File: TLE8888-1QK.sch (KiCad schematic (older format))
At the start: 40 parts, among them Q1 IPD30N06S2L-23, U2 TLE8888QK

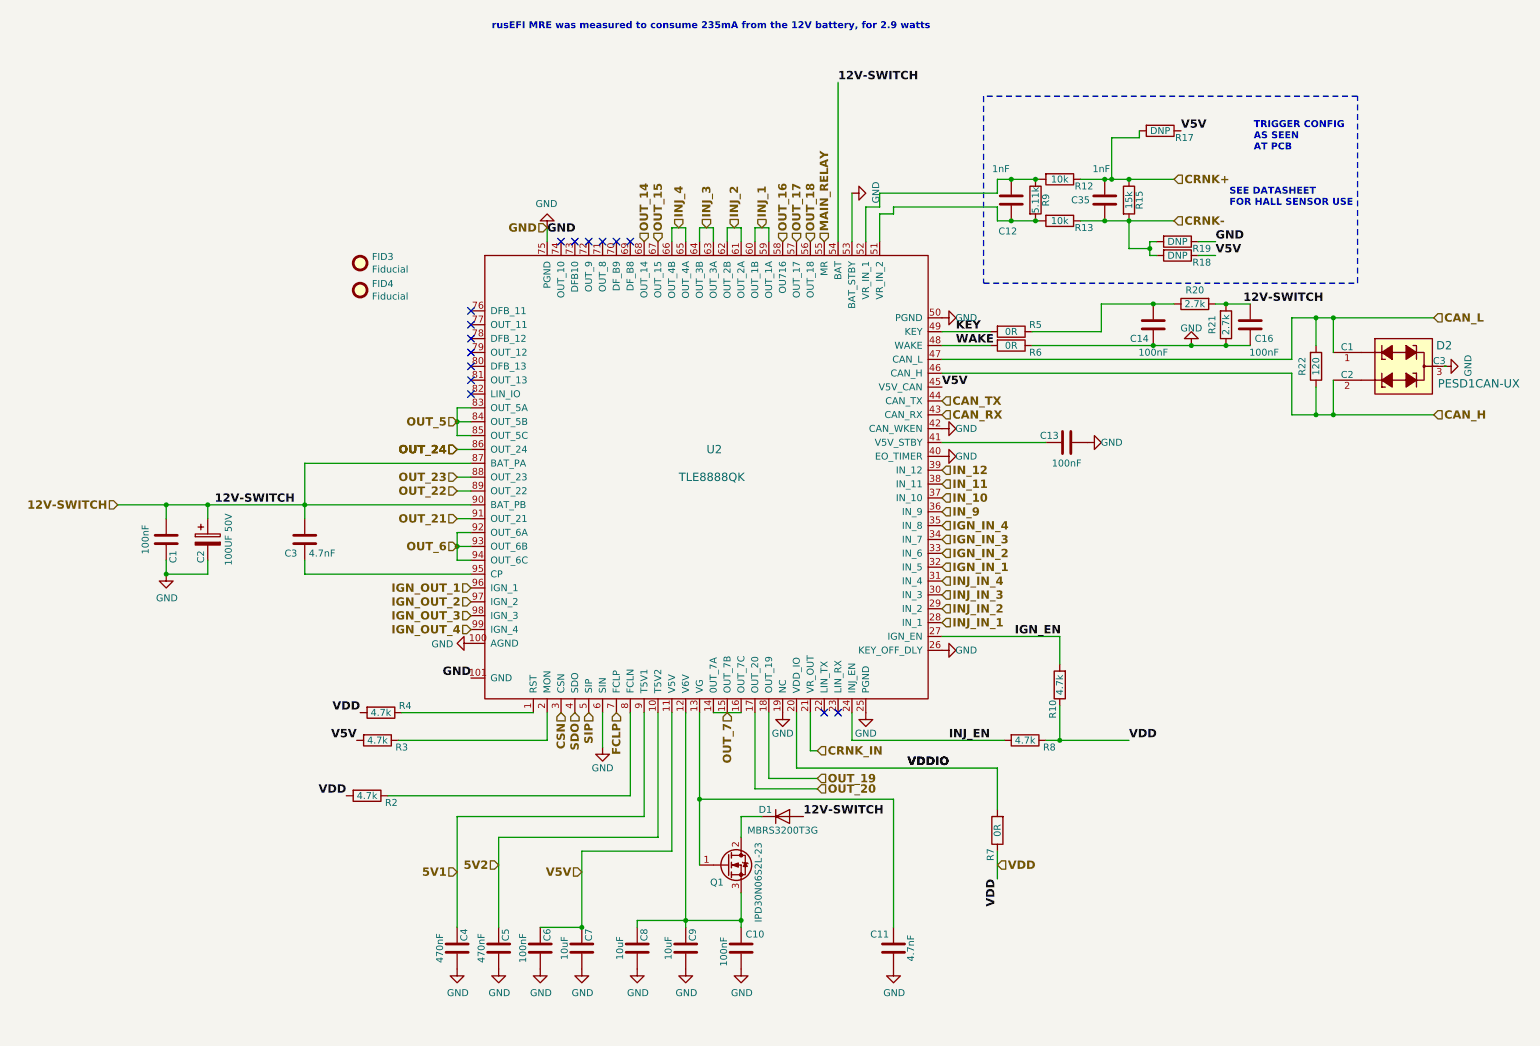
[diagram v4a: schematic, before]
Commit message: Significant revision of schematic and layout:
Added reverse voltage protection.
Split 12V supply into a 12V-Key (ignition) pin and a 12V-MRel (supply from
main relay) pin.  The 12V main relay is controlled by the MRel pin to protect against reverse voltage and over-voltage.

The board can optionally draw under 1mA from the main relay coil to power
standby features, including CAN monitoring.

Increased the size of several resistors, notably ignition output resistors
and CAN termination, to handle typical power draw.

Changed resistor dividers to individual resistors for better accuracy than
typical resistor networks.

Standardized pull-up and pull-down resistors to 10K.

Changed to a tab-output regulator.
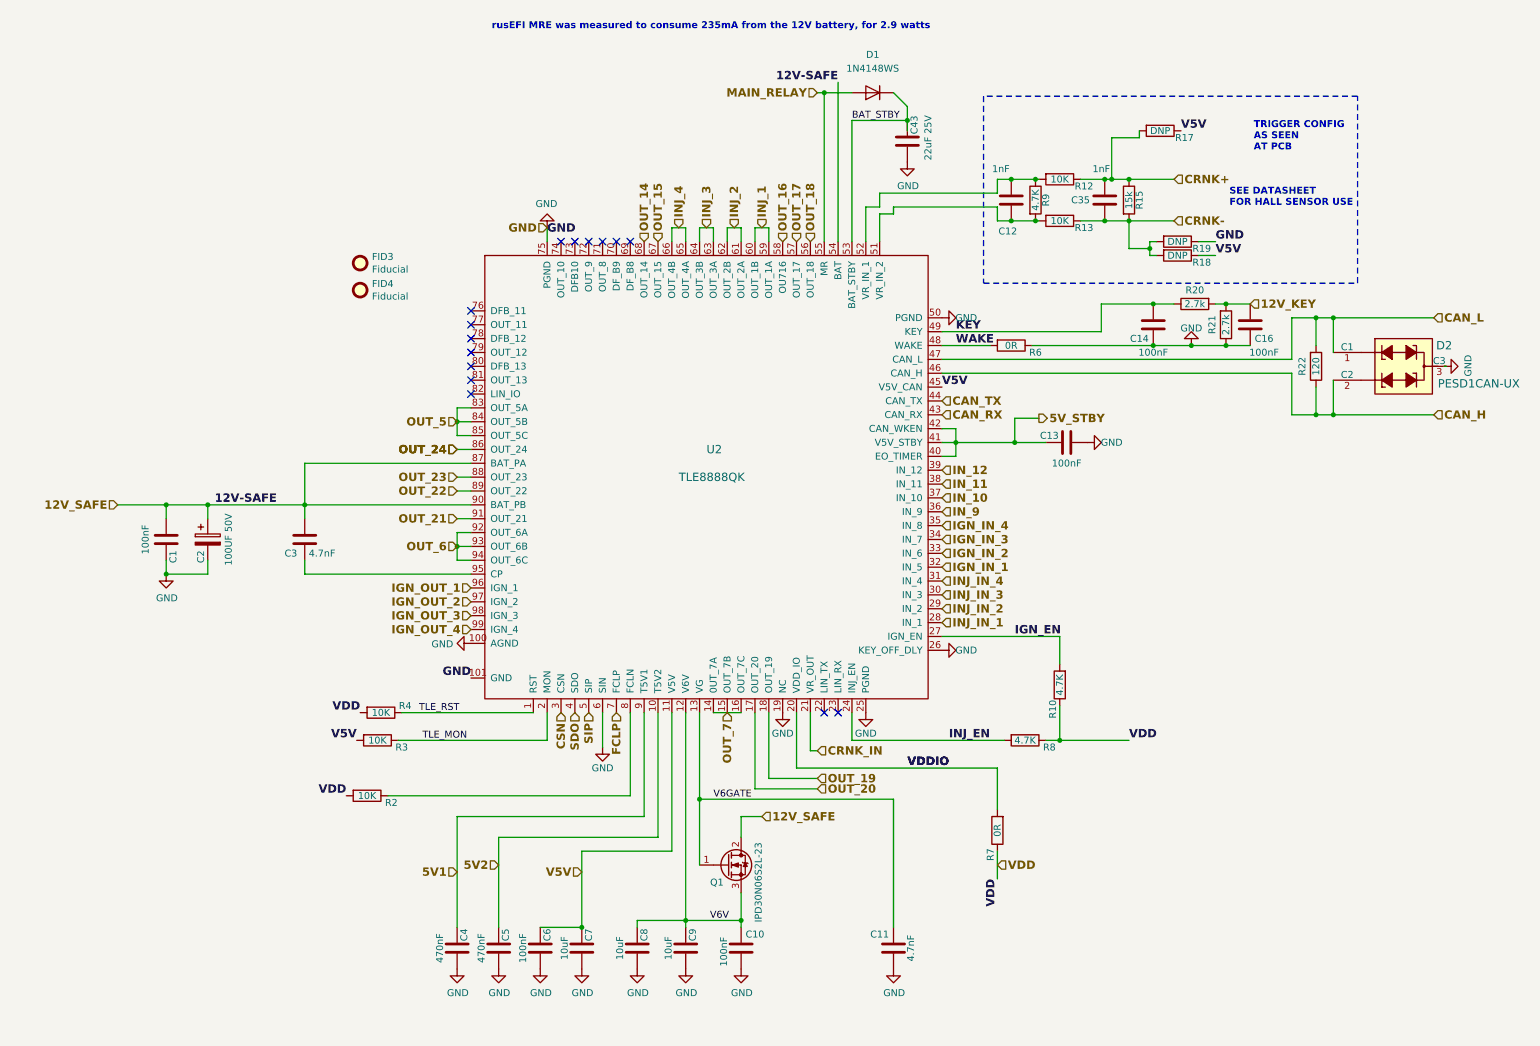
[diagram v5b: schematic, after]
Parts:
- removed D1: MBRS3200T3G, Diode_SMD:D_SMB, symbol Device:D
- removed R5: 0R, Resistor_SMD:R_0603_1608Metric, symbol Device:R
- added C43: 22uF 25V, Capacitor_SMD:C_0805_2012Metric, symbol Device:C
- added D1: 1N4148WS, Diode_SMD:D_SOD-323, symbol Diode:1N4148WS
- C1, C10, C13, C14, C16, C6: LCSC (none) -> C14663
- C11, C3: LCSC (none) -> C53987
- C12, C35: LCSC (none) -> C1588
- C4, C5: LCSC (none) -> C1623
- C7, C8, C9: LCSC (none) -> C19702
- R10, R8: value 4.7k -> 4.7K; LCSC (none) -> C23162
- R12, R13: value 10k -> 10K; LCSC (none) -> C25804
- R15: LCSC (none) -> C22809
- R2, R3, R4: value 4.7k -> 10K; LCSC (none) -> C25804; Manufacturer StackPole -> (none); Part # RMCF0603JT4K70 -> (none); VEND DIGI -> (none); VEND# RMCF0603JT4K70CT-ND -> (none)
- R20, R21: LCSC (none) -> C13167
- R22: footprint Resistor_SMD:R_0603_1608Metric -> Resistor_SMD:R_0805_2012Metric; LCSC (none) -> C17437; Manufacturer StackPole -> (none); Part # RMCF0603JG120R -> (none); VEND DIGI -> (none); VEND# RMCF0603JG120RCT-ND -> (none)
- R6, R7: LCSC (none) -> C21189
- R9: value 5.11k -> 4.7K; LCSC (none) -> C23162; Manufacturer StackPole -> (none); Part # RMCF0603FT5K11 -> (none); VEND DIGI -> (none); VEND# RMCF0603FT5K11CT-ND -> (none)
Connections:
- net GND: now also C43.2; no longer U2.40 (EO_TIMER), U2.42 (CAN_WKEN), U2.53 (BAT_STBY)
- net KEY: now also C14.1, R20.1
- net MAIN_RELAY: now also D1.2 (A)
- net TLE_RST: now reaches R4.1, U2.1 (RST)
- net V6V: now reaches C10.1, C8.1, C9.1, Q1.3 (S), U2.12 (V6V)
- net V6GATE: now reaches C11.1, Q1.1 (G), U2.13 (VG)
- net TLE_MON: now reaches R3.1, U2.2 (MON)
- net 5V_STBY: now reaches C13.1, U2.41 (V5V_STBY)
- net 5V_STBY: now also U2.40 (EO_TIMER), U2.42 (CAN_WKEN)
- net 12V_SAFE: now reaches Q1.2 (D)
- net 12V_SAFE: now also C1.1, C2.1, C3.1, U2.54 (BAT), U2.87 (BAT_PA), U2.90 (BAT_PB)
- removed net 12V-SWITCH: C1.1, C16.1, C2.1, C3.1, R20.2, R21.2, U2.54 (BAT), U2.87 (BAT_PA), U2.90 (BAT_PB)
- new net 12V_KEY: C16.1, R20.2, R21.2
- new net BAT_STBY: C43.1, D1.1 (K), U2.53 (BAT_STBY)

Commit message: Includes all known errata, except for component rotation for JLCPCB fabrication.
Includes
  Refined reverse protection layout with dual SS54 diodes
  Load dump protection, SMB TVS for 33V TVS
  Multiple footprints for Flash (SO-16, SO-8-208 and SO-8-150)
  Simplified pull-up and pull-down resistors, omitting unneeded ones
  Individual resistors for resistor dividers for easier sourcing of
    1% precision (most resistor networks are 5%, most 0603 parts are 1%).
  PicoBlade connector for RTC battery, matches low-cost laptop 2032 cells
  Clamping diode arrays on top, alternate BAS70 on bottom
  Options for VR input modification, and analog pull-ups on bottom.
  LM1117 voltage regulator footprint
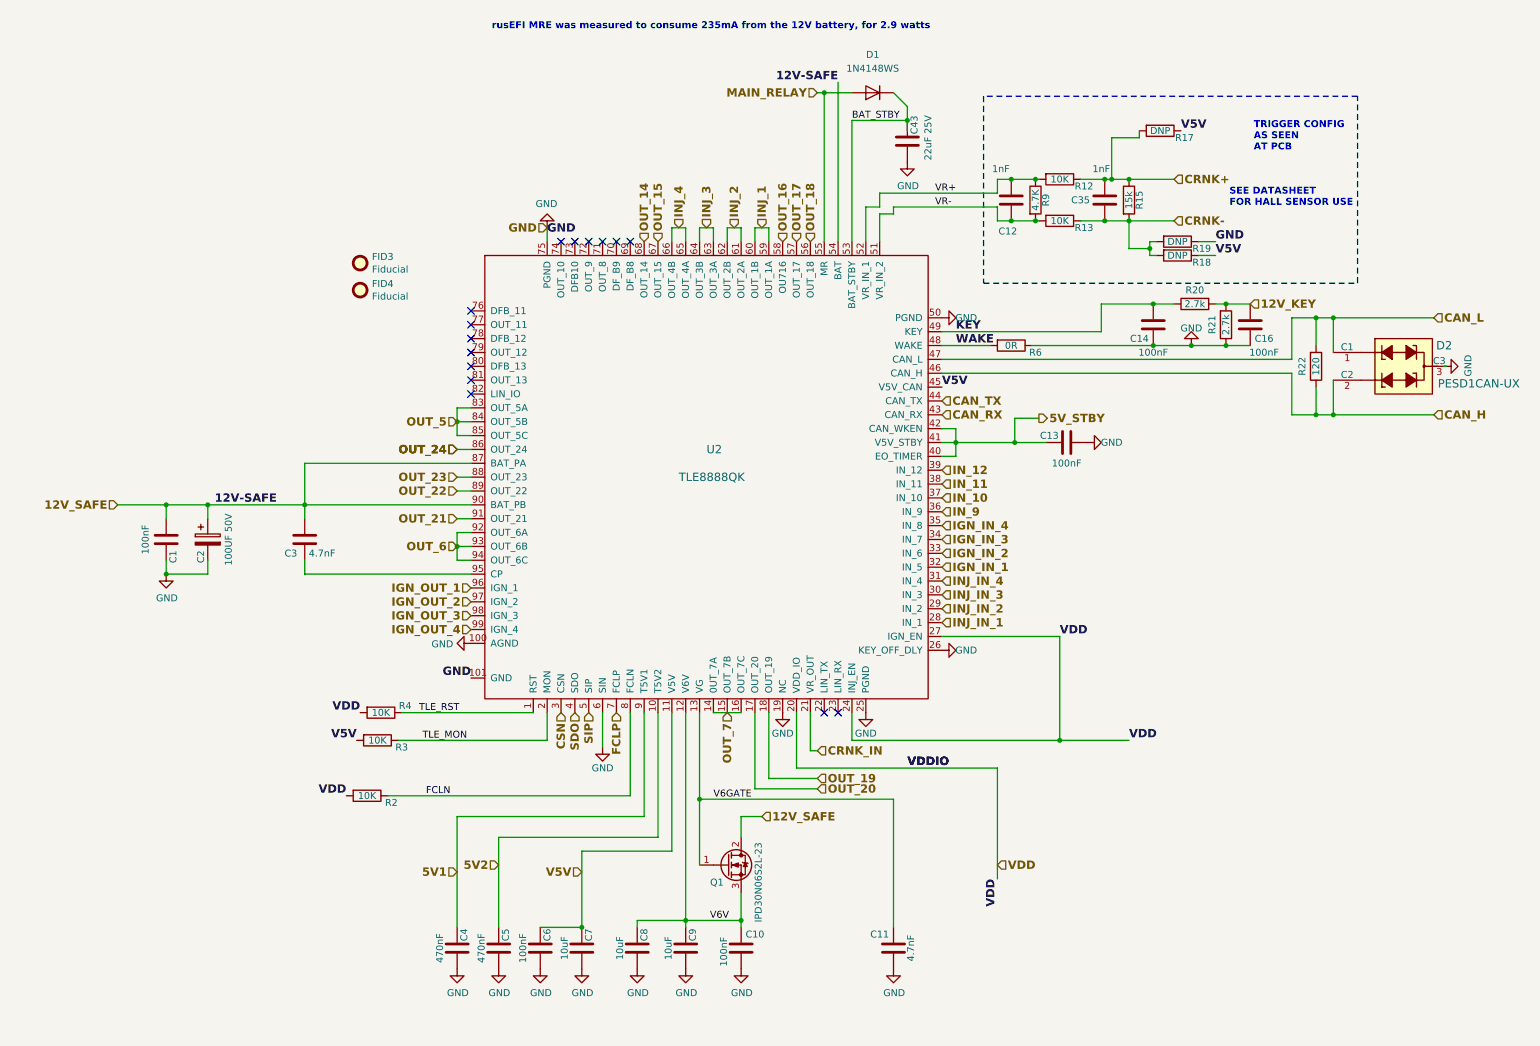
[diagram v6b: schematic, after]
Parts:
- removed R10, R8: 4.7K, Resistor_SMD:R_0603_1608Metric, symbol Device:R
- removed R7: 0R, Resistor_SMD:R_0603_1608Metric, symbol Device:R
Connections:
- net IGN_EN is gone; now on net VDD: U2.27 (IGN_EN)
- net INJ_EN is gone; now on net VDD: U2.24 (INJ_EN)
- net VDDIO is gone; now on net VDD: U2.20 (VDD_IO)
- net VR-: now reaches C12.2, R13.2, R9.2, U2.51 (VR_IN_2)
- net VR+: now reaches C12.1, R12.2, R9.1, U2.52 (VR_IN_1)
- net FCLN: now reaches R2.1, U2.8 (FCLN)
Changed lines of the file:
@@
 Sheet 2 7
 Title "microRusEfi"
-Date "2019-07-01"
-Rev "R0.2"
+Date "2019-09-24"
+Rev "R0.4.2"
 Comp ""
 Comment1 ""
@@
 Text Label 11600 7450 0    60   ~ 12
 WAKE
-Text Label 12025 9550 0    60   ~ 12
-IGN_EN
-Text Label 11550 10300 0    60   ~ 12
-INJ_EN
 Text Label 8100 9850 2    60   ~ 12
 GND
@@
 	13025 7450 13300 7450
 Connection ~ 13300 7450
-$Comp
-L Device:R R7
-U 1 1 5CA0441A
-P 11900 10950
-F 0 "R7" V 11950 11125 50  0000 C CNN
-F 1 "0R" V 11900 10950 50  0000 C CNN
-F 2 "Resistor_SMD:R_0603_1608Metric" V 11830 10950 50  0001 C CNN
-F 3 "~" H 11900 10950 50  0001 C CNN
-F 4 "DIGI" H 3900 250 50  0001 C CNN "VEND"
-F 5 "RMCF0603ZT0R00" H 0   0   50  0001 C CNN "Part #"
-F 6 "RMCF0603ZT0R00CT-ND" H 0   0   50  0001 C CNN "VEND#"
-F 7 "StackPole" H 0   0   50  0001 C CNN "Manufacturer"
-F 8 "C21189" H 11900 10950 50  0001 C CNN "LCSC"
-	1    11900 10950
-	-1   0    0    1
-$EndComp
-Wire Wire Line
-	11900 11100 11900 11300
 Wire Wire Line
 	10450 10500 11900 10500
-Wire Wire Line
-	11900 10500 11900 10800
 Text Label 12850 10300 0    60   ~ 12
 VDD
@@
 Text Label 7300 10100 2    60   ~ 12
 VDD
-Wire Wire Line
-	10850 10300 11950 10300
-$Comp
-L Device:R R8
-U 1 1 5CA13776
-P 12100 10300
-F 0 "R8" V 12150 10475 50  0000 C CNN
-F 1 "4.7K" V 12100 10300 50  0000 C CNN
-F 2 "Resistor_SMD:R_0603_1608Metric" V 12030 10300 50  0001 C CNN
-F 3 "~" H 12100 10300 50  0001 C CNN
-F 4 "DIGI" H 4100 -400 50  0001 C CNN "VEND"
-F 5 "RMCF0603JT4K70" H 0   0   50  0001 C CNN "Part #"
-F 6 "RMCF0603JT4K70CT-ND" H 0   0   50  0001 C CNN "VEND#"
-F 7 "StackPole" H 0   0   50  0001 C CNN "Manufacturer"
-F 8 "C23162" H 12100 10300 50  0001 C CNN "LCSC"
-	1    12100 10300
-	0    1    1    0
-$EndComp
-$Comp
-L Device:R R10
-U 1 1 5CA15AC9
-P 12350 9900
-F 0 "R10" V 12400 10075 50  0000 C CNN
-F 1 "4.7K" V 12350 9900 50  0000 C CNN
-F 2 "Resistor_SMD:R_0603_1608Metric" V 12280 9900 50  0001 C CNN
-F 3 "~" H 12350 9900 50  0001 C CNN
-F 4 "DIGI" H 4350 -800 50  0001 C CNN "VEND"
-F 5 "RMCF0603JT4K70" H 0   0   50  0001 C CNN "Part #"
-F 6 "RMCF0603JT4K70CT-ND" H 0   0   50  0001 C CNN "VEND#"
-F 7 "StackPole" H 0   0   50  0001 C CNN "Manufacturer"
-F 8 "C23162" H 12350 9900 50  0001 C CNN "LCSC"
-	1    12350 9900
-	-1   0    0    1
-$EndComp
-Wire Wire Line
-	12350 9550 12350 9750
-Wire Wire Line
-	12350 10050 12350 10300
-Wire Wire Line
-	12250 10300 12350 10300
 Wire Wire Line
 	8650 10100 8650 10300
@@
 Text Label 7750 10300 0    50   ~ 0
 TLE_MON
+Text Label 11450 6350 0    50   ~ 0
+VR+
+Text Label 11450 6450 0    50   ~ 0
+VR-
+Text Label 12350 9550 0    60   ~ 12
+VDD
+Wire Wire Line
+	12350 9550 12350 10300
+Wire Wire Line
+	10850 10300 12350 10300
+Wire Wire Line
+	11900 10500 11900 11300
+Text Label 7775 10700 0    50   ~ 0
+FCLN
 $EndSCHEMATC

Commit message: Added 2x5 header for SPI/serial communications Connected LIN to PD8/PD9 USART3, output on SMD testpoint. Added standby regulator. Changed footprints of reverse protection diodes to SMA. Rotated two opamps and clamping diode arrays for cleaner layout. Moved status LEDs over for better silkscreen labels. Moved CAN termination and TVS to lower right.
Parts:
- removed C16: 100nF, Capacitor_SMD:C_0603_1608Metric, symbol Device:C
- removed R21: 2.7k, Resistor_SMD:R_0603_1608Metric, symbol Device:R
- added C41: 2.2uF, Capacitor_SMD:C_0603_1608Metric, symbol Device:C
- D1: value 1N4148WS -> BAV70; footprint Diode_SMD:D_SOD-323 -> Package_TO_SOT_SMD:SOT-23; symbol Diode:1N4148WS -> Diode:BAV70; LCSC C2128 -> C68978
- D2: footprint Package_TO_SOT_SMD:SOT-323_SC-70_Handsoldering -> Package_TO_SOT_SMD:SOT-23
- R6: value 0R -> 10K; LCSC C21189 -> C25804; Manufacturer StackPole -> (none); Part # RMCF0603ZT0R00 -> (none); VEND DIGI -> (none); VEND# RMCF0603ZT0R00CT-ND -> (none)
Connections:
- net labels added: LIN_IO, LIN_RX, LIN_TX
- wire segments 163 -> 170
- no-connect marks 15 -> 12
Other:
- moved on the sheet: C10, C11, C8, C9, Q1

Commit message: 0.4.5-2L board as submitted for fabrication
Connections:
- net labels added: DFB10, DFB8, DFB9, OUT_10, OUT_8, OUT_9
- wire segments 170 -> 165
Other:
- note added: "VR INPUT ADJUSTMENT\nR17, R18, R19, R9, C12\nON BOTTOM LAYER"
- note removed: "TRIGGER CONFIG\nAS SEEN\nAT PCB"
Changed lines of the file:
@@
 Sheet 7 7
 Title "microRusEfi-2L"
-Date "2019-10-06"
+Date "2019-10-08"
 Rev "R0.4.5"
 Comp "rusEFI.com"
@@
 Text HLabel 8650 6600 0    60   Input ~ 12
 GND
-Text Label 8650 6650 0    60   ~ 12
-GND
 Wire Wire Line
 	6900 9100 8100 9100
@@
 Connection ~ 12850 6550
 Wire Wire Line
-	12925 5950 12725 5950
-Wire Wire Line
-	12925 5950 12925 5900
+	12725 5900 12925 5900
 Wire Wire Line
 	13000 6800 13050 6800
@@
 	13000 6750 13000 6800
 Wire Wire Line
-	10950 6450 11050 6450
-Wire Wire Line
-	11050 6450 11050 6350
-Wire Wire Line
-	10950 6450 10950 6700
-Wire Wire Line
-	11050 6700 11050 6500
-Wire Wire Line
-	11050 6500 11150 6500
-Wire Wire Line
-	11150 6500 11150 6450
-Wire Wire Line
-	12725 5950 12725 6250
-Wire Wire Line
 	12850 6550 12850 6750
 Wire Notes Line
@@
 Wire Notes Line
 	14500 7000 14500 5650
-Text Notes 13750 6050 0    50   ~ 10
-TRIGGER CONFIG\nAS SEEN\nAT PCB
+Text Notes 13525 6050 0    50   ~ 10
+VR INPUT ADJUSTMENT\nR17, R18, R19, R9, C12\nON BOTTOM LAYER
 Text Label 13475 6800 0    60   ~ 12
 V5V
@@
 Wire Wire Line
 	11600 8150 12025 8150
-Wire Wire Line
-	11150 6450 11900 6450
-Wire Wire Line
-	11050 6350 11900 6350
 $Comp
 L rusefi_tle8888:TLE8888QK U2
@@
 	-1   0    0    -1
 $EndComp
+Wire Wire Line
+	12725 5900 12725 6250
+Wire Wire Line
+	10950 6350 10950 6700
+Wire Wire Line
+	10950 6350 11900 6350
+Wire Wire Line
+	11050 6450 11050 6700
+Wire Wire Line
+	11050 6450 11900 6450
+Text Label 9250 6700 1    50   ~ 10
+DFB8
+Text Label 9150 6700 1    50   ~ 10
+DFB9
+Text Label 9050 6700 1    50   ~ 10
+OUT_8
+Text Label 8950 6700 1    50   ~ 10
+OUT_9
+Text Label 8850 6700 1    50   ~ 10
+DFB10
+Text Label 8750 6700 1    50   ~ 10
+OUT_10
 $EndSCHEMATC
